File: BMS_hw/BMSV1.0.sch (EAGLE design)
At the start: 191 parts, among them IC1 MC33771BEP, IC2 SFH6156, IC3 MIC28515V1, J2 NTC, Q1 IRLML5203, T1 IPT020N10N3V1, T2 IPT020N10N3V1, T3 IPT020N10N3V1, T4 IPT020N10N3V1, X2 87758-1816

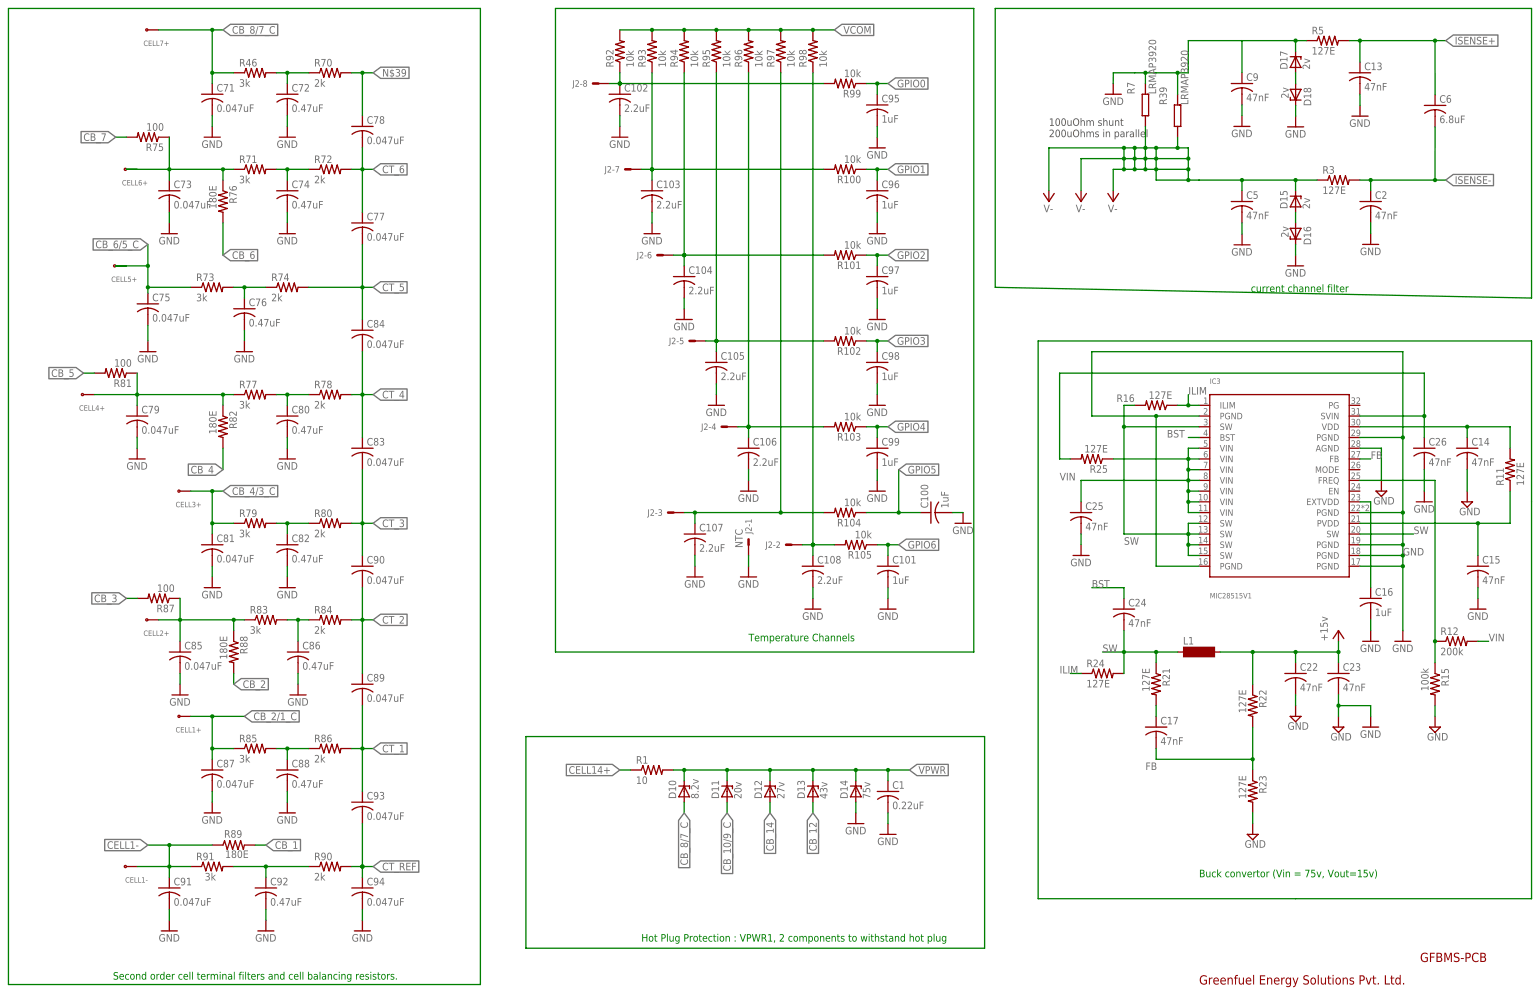
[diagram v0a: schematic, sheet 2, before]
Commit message: Invalid polygon in gf board
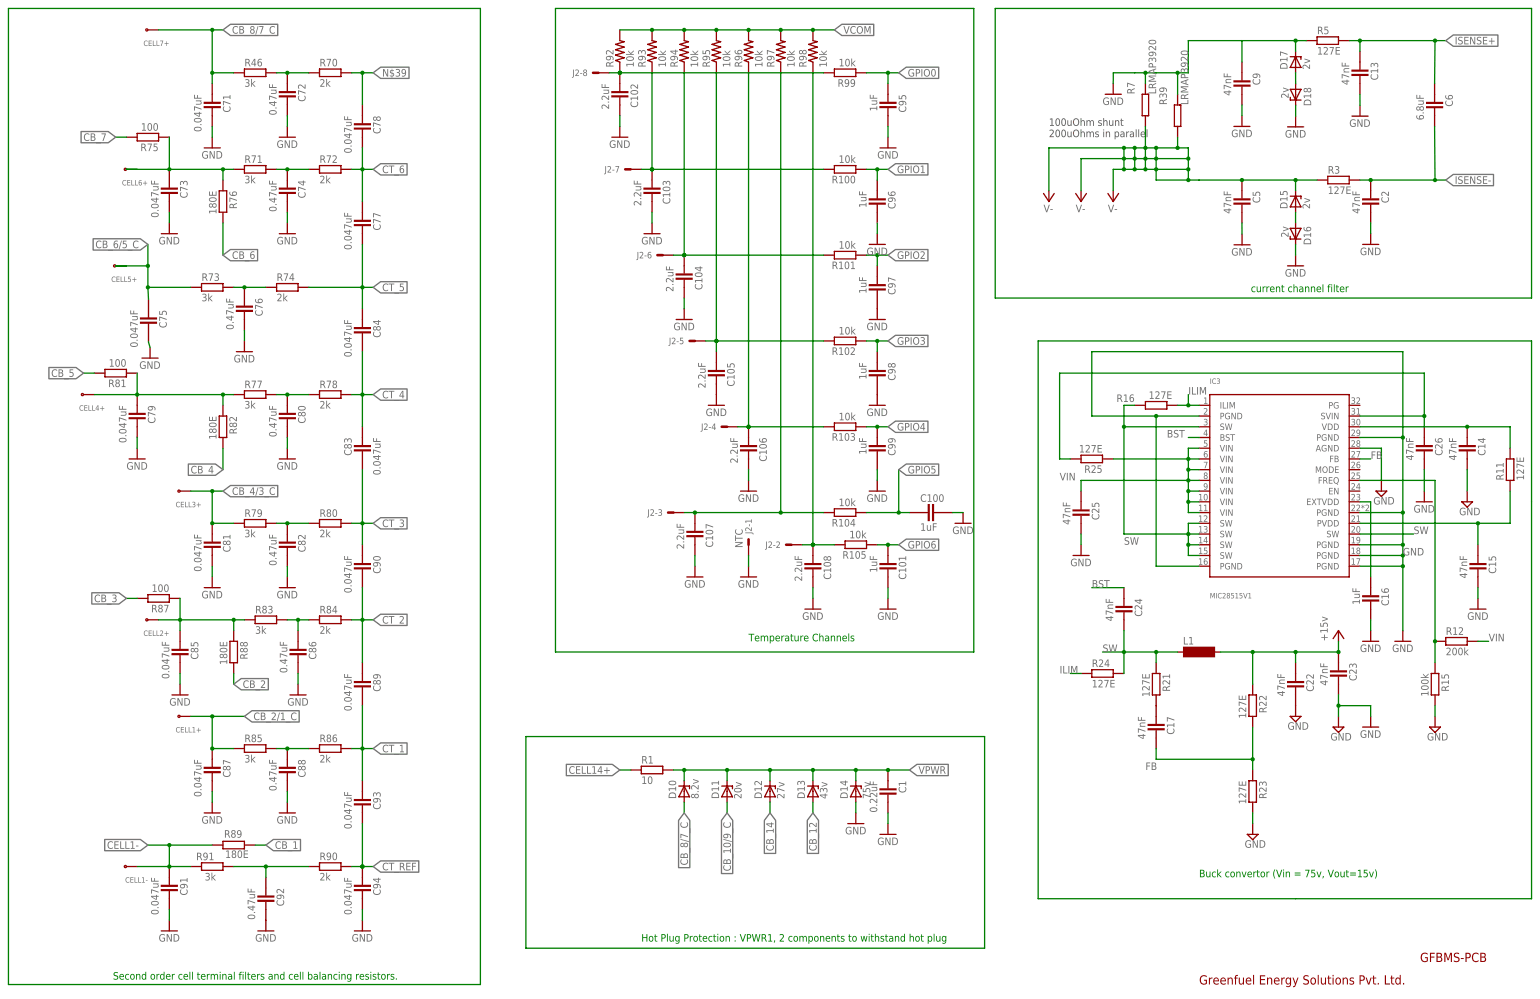
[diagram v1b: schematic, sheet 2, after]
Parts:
- added IC4, IC5, IC6: FOD8384-COC, GreenFuel:FOD8384-COC
- added Q2: IRLML5203, transistor-power:IRLML5203
- added R40, R41, R42, R8: 10k, ipc-7351-resistor:RESISTOR_0402
- added X1, X4: 87758-2016, con-molex:87758-2016
- C1, C10, C100, C101, C102, C103, C104, C105, C106, C107, C108, C11, C12, C13, C14, C15, C16, C17, C18, C19, C2, C20, C21, C22, C23, C24, C25, C26, C27, C28, C29, C3, C31, C32, C33, C34, C35, C36, C37, C4, C5, C6, C66, C67, C7, C71, C72, C73, C74, C75, C76, C77, C78, C79, C8, C80, C81, C82, C83, C84, C85, C86, C87, C88, C89, C9, C90, C91, C92, C93, C94, C95, C96, C97, C98, C99: device adafruit:C-USC0805 -> ipc-7351-capacitor:CAPACITOR_0402
- R1, R10, R100, R101, R102, R103, R104, R105, R11, R12, R13, R14, R15, R16, R17, R18, R19, R2, R20, R21, R22, R23, R24, R25, R26, R27, R28, R29, R3, R30, R31, R32, R33, R34, R35, R36, R37, R38, R4, R46, R5, R6, R64, R66, R67, R70, R71, R72, R73, R74, R75, R76, R77, R78, R79, R80, R81, R82, R83, R84, R85, R86, R87, R88, R89, R9, R90, R91, R99: device adafruit:R-US_R0805 -> ipc-7351-resistor:RESISTOR_0402
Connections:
- removed net N$29: T1.D, T2.D, T3.D, T4.D
- new net 15V_AUX: IC4.VDD, IC5.VDD, IC6.VDD, X1-17.S, X4-17.S
- new net CHG_FET: IC4.ANODE
- new net C_FET: X1-9.S, X4-9.S
- new net DSG_FET: IC6.ANODE
- new net D_FET: X1-19.S, X4-19.S
- new net FAULT: X1-5.S, X4-5.S
- new net ISP: X1-11.S, X4-11.S
- new net N$20: IC4.CATHODE, R8.1
- new net N$25: IC6.CATHODE, R40.1
- new net N$27: IC5.CATHODE, R41.1
- new net N$28: Q2.D, R42.2
- new net N$38: IC5.VO
- new net PCHG_FET: IC5.ANODE, Q2.G, X1-4.S, X4-4.S
- new net PWR_DRAIN: Q2.S, T1.D, T2.D, T3.D, T4.D
- new net VBATT-: R42.1
- new net VDD: X1-12.S, X1-13.S, X4-12.S, X4-13.S
- net CHG_GATE: now also IC6.VO
- net DSG_GATE: now also IC4.VO
- net GND: now also IC4.VSS, IC5.VSS, IC6.VSS, R40.2, R41.2, R8.2, X1-1.S, X1-10.S, X1-14.S, X1-15.S, X1-16.S, X1-18.S, X1-2.S, X1-20.S, X1-3.S, X1-6.S, X1-7.S, X1-8.S, X4-1.S, X4-10.S, X4-14.S, X4-15.S, X4-16.S, X4-18.S, X4-2.S, X4-20.S, X4-3.S, X4-6.S, X4-7.S, X4-8.S
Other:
- moved on the sheet: C1, C10, C100, C101, C102, C103, C104, C105, C106, C107, C108, C11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

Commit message: board finnnnalo
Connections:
- removed net N$39: C78.1, R70.2
- net CT_7: now also C78.1, R70.2
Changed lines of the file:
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@@
 </segment>
 </net>
-<net name="N$39" class="0">
+<net name="CT_7" class="0">
 <segment>
 <pinref part="R70" gate="G$1" pin="2"/>

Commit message: sch brd lib placment comptd!
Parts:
- added D3, D4, D5: SFH48225, GreenFuel:SFH48225
- added JP1: (no value), GreenFuel:PINOLED-4
- added LED1: L-59EGW-CAGR, GreenFuel:L-59EGW-CAGR
- added R43, R44, R45, R47, R48, R49, R50, R51, R52, R53, R54, R55, R56, R57, R58: (no value), ipc-7351-resistor:RESISTOR_0402
- added R59, R60, R61, R62: 10k, ipc-7351-resistor:RESISTOR_0402
- L1: value (none) -> XAL1010-822MEB; device inductor-neosid:MS85 -> GreenFuel:XAL1010-822MEB
- R39, R7: value LRMAP3920 -> LRMAP3920SUNT; device GreenFuel:LRMAP3920 -> GreenFuel:LRMAP3920SUNT
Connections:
- new net 3.3V: JP1.3, R59.2, X1-16.S
- new net N$29: CELL14+.S, R43.1
- new net N$33: CELL6+.S, R49.1
- new net N$35: CELL5+.S, R50.1
- new net N$37: CELL12+.S, R44.1
- new net N$39: CELL10+.S, R45.1
- new net N$40: CELL8+.S, R47.1
- new net N$43: CELL7+.S, R48.1
- new net N$58: CELL4+.S, R51.1
- new net N$59: CELL3+.S, R54.1
- new net N$60: CELL2+.S, R52.1
- new net N$62: CELL1+.S, R55.1
- new net N$63: CELL1-.S, R53.1
- new net N$64: CELL11+.S, R56.1
- new net N$65: CELL13+.S, R57.1
- new net N$66: CELL9+.S, R58.2
- new net N$68: C9.1, R39.5, R7.5
- new net N$70: C5.1, D15.C, R3.1, R39.2, R7.2
- new net N$71: LED1.A, R59.1
- new net N$72: D4.C, R62.1
- new net N$73: D5.C, R60.1
- new net N$74: D3.C, R61.1
- new net OLED_SCL: JP1.2, X1-6.S
- new net OLED_SDA: JP1.1, X1-4.S
- new net RDTX_OUT+: IC1.RDTX_OUT+, X1-5.S
- new net RDTX_OUT-: IC1.RDTX_OUT-, X1-9.S
- new net S-LED_1: LED1.CR, X1-11.S
- new net S-LED_2: LED1.CG, X1-13.S
- new net S-LED_3: D3.A, X1-15.S
- new net S-LED_4: D5.A, X1-17.S
- new net S-LED_5: D4.A, X1-19.S
- net 15V_AUX: no longer X1-17.S
- net CB_10/9_C: now also R58.1; no longer CELL9+.S
- net CB_12/11_C: now also R56.2; no longer CELL11+.S
- net CB_13/12_C: now also R44.2; no longer CELL12+.S
- net CB_13/12_C1: now also R45.2; no longer CELL10+.S
- net CB_13/12_C2: now also R47.2; no longer CELL8+.S
- net CB_13/12_C6: now also R49.2; no longer CELL6+.S
- net CB_13/12_C7: now also R51.2; no longer CELL4+.S
- net CB_13/12_C8: now also R52.2; no longer CELL2+.S
- net CB_14/13_C: now also R57.2; no longer CELL13+.S
- net CB_2/1_C: now also R55.2; no longer CELL1+.S
- net CB_4/3_C: now also R54.2; no longer CELL3+.S
- net CB_6/5_C: now also R50.2; no longer CELL5+.S
- net CB_8/7_C: now also R48.2; no longer CELL7+.S
- net CELL1-: now also R53.2; no longer CELL1-.S
- net CELL14+: now also R43.2; no longer CELL14+.S
- net C_FET: no longer X1-9.S
- net D_FET: no longer X1-19.S
- net FAULT: no longer X1-5.S
- net GND: now also JP1.4, R39.4, R60.2, R61.2, R62.2, R7.4; no longer C9.1, IC1.RDTX_OUT+, IC1.RDTX_OUT-, R39.P$2, R7.P$2, X1-15.S, X1-16.S, X1-6.S
- net ISP: no longer X1-11.S
- net PCHG_FET: no longer X1-4.S
- net V-: now also R39.1, R7.1; no longer C5.1, D15.C, R3.1, R39.P$1, R7.P$1
- net VDD: no longer X1-13.S
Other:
- note added: "Read out ways >>OLED >>LED's"
- moved on the sheet: C5, C67, CELL1+, CELL1-, CELL10+, CELL11+, CELL12+, CELL13+, CELL14+, CELL2+, CELL3+, CELL4+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

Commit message: brd lbr sch updated to new version
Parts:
- D10, D11, D12, D13, D14, D15, D16, D17, D18: device diode:ZENER-DIODESOD80C -> ipc-7351-diode:SCHOTTKY_SOD-123
- R92, R93, R94, R95, R96, R97, R98: device adafruit:R-US_R0805 -> ipc-7351-resistor:RESISTOR_0402
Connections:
- removed net N$15: D17.C, R5.1
- net GND: now also D16.K, D18.K; no longer D16.C, D18.C
- net N$68: now also D17.K, R5.1
- net N$70: now also D15.K; no longer D15.C
- net VPWR: now also D10.K, D11.K, D12.K, D13.K, D14.K; no longer D10.C, D11.C, D12.C, D13.C, D14.C
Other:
- moved on the sheet: R5, R74

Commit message: placment 80% done
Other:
- note added: "FET optoisolated, drivers and precharge circuit"
- note added: "Piggy board connectors !"
- moved on the sheet: D3, D4, D5, JP1, LED1, R59, R60, R61, R62

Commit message: buck routing complete !
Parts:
- added C30: (no value), ipc-7351-capacitor:CAPACITOR_0402
- added D19, D7, D8, D9: (no value), ipc-7351-diode:SCHOTTKY_SOD-123
- added D6: (no value), ipc-7351-diode:ZENER_SOD-123
- added JP2, JP3: (no value), adafruit:PINHD-1X1CB
- added R63, R65: 10k, ipc-7351-resistor:RESISTOR_0402
- added X3: 22-23-2041, GreenFuel:22-23-2041
- added X5: 22-23-2051, GreenFuel:22-23-2051
- C14, C15: value 47nF -> 2.2uF
- C22: device ipc-7351-capacitor:CAPACITOR_0402 -> ipc-7351-capacitor:CAPACITOR_0603
- C23, C25: device ipc-7351-capacitor:CAPACITOR_0402 -> ipc-7351-capacitor:CAPACITOR_1210
- D1: device diode:ZENER-DIODESOD80C -> ipc-7351-diode:ZENER_SOD-123
- D2: value GF1 -> (none); device diode:GF1 -> ipc-7351-diode:DIODE_SOD-123
- R11: value 127E -> 2E2
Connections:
- net N$16 renamed PVDD
- removed net N$10: C14.1, IC3.VDD, R11.2
- new net !MCLR: X4-10.S, X5-5.S
- new net CANH: D19.K, X3-4.S
- new net CANL: D9.K, X3-3.S
- new net INTL_IN2: D7.A, X3-1.S
- new net INTL_OUT1: JP3.1, X3-2.S
- new net KEY-IN: D7.K, D8.K, R63.1
- new net N$78: D8.A, JP2.1
- new net RX_O: X4-14.S, X5-2.S
- new net TX_O: X4-16.S, X5-3.S
- new net WAKE: C30.2, D6.K, R63.2, R65.1
- net 3.3V: now also X4-12.S, X5-4.S
- net GND: now also C30.1, D19.A, D6.A, D9.A, R65.2, X5-1.S; no longer X4-10.S, X4-14.S, X4-16.S
- net N$23: now also D1.K, D2.K; no longer D1.C, D2.C
- net N$29: now also C25.1, IC3.VIN, IC3.VIN@1, IC3.VIN@2, IC3.VIN@3, IC3.VIN@4, IC3.VIN@5, IC3.VIN@6, R25.1
- net VDD: now also C14.1, IC3.VDD, R11.2; no longer X4-12.S
- net VIN: no longer C25.1, IC3.VIN, IC3.VIN@1, IC3.VIN@2, IC3.VIN@3, IC3.VIN@4, IC3.VIN@5, IC3.VIN@6, R25.1
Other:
- note added: "Key-In and wake up module"
- note added: "UART and CAN connector"
- moved on the sheet: X1-1, X1-10, X1-11, X1-12, X1-13, X1-14, X1-15, X1-16, X1-17, X1-18, X1-19, X1-2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
